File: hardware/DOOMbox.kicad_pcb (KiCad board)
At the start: 4 copper layers, 128 parts, among them J1 DE15_Socket_HighDensity, J2 AudioJack3, SW1 SW_SPST, SW2 SW_Push, U1 RPi Pico 2, U2 AP7381-50SA-7, U3 LM324N, U4 CD4010BE

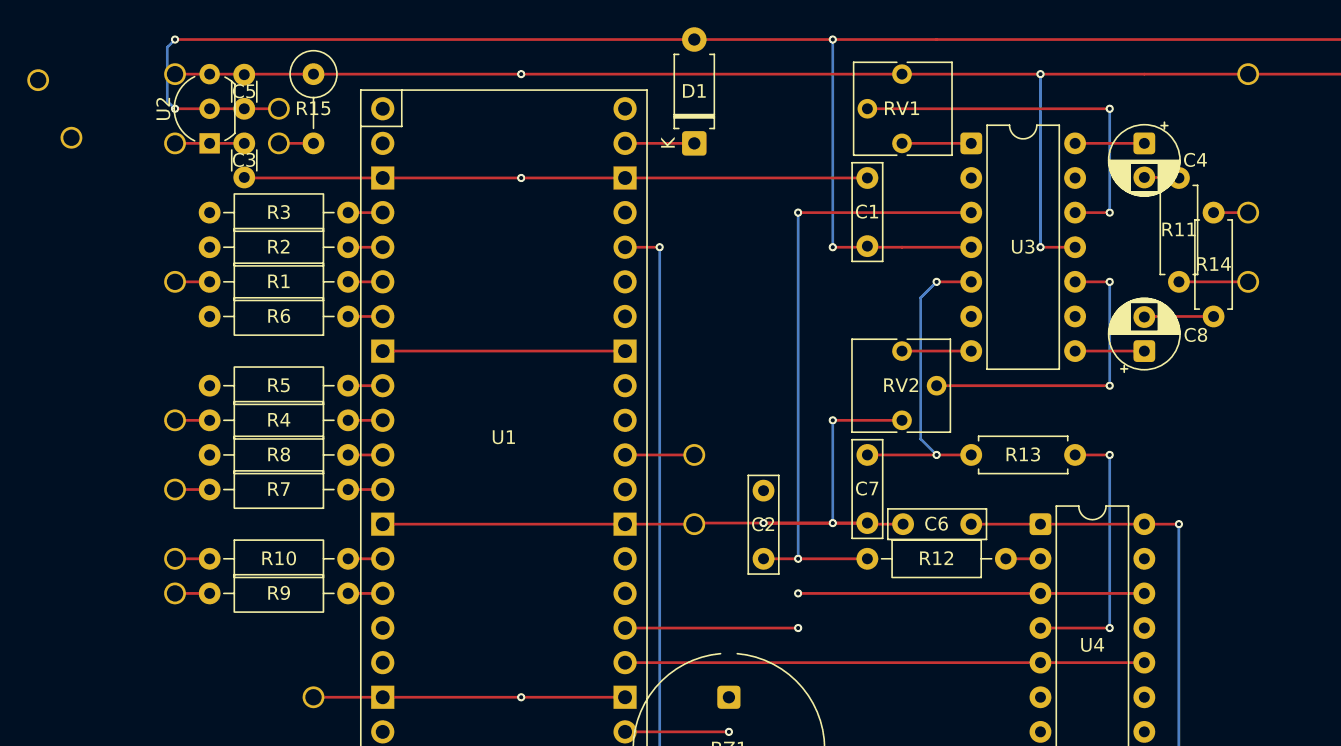
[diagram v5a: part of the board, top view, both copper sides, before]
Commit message: Fix incorrect pins on U2 and accidental stripboard cut in U4
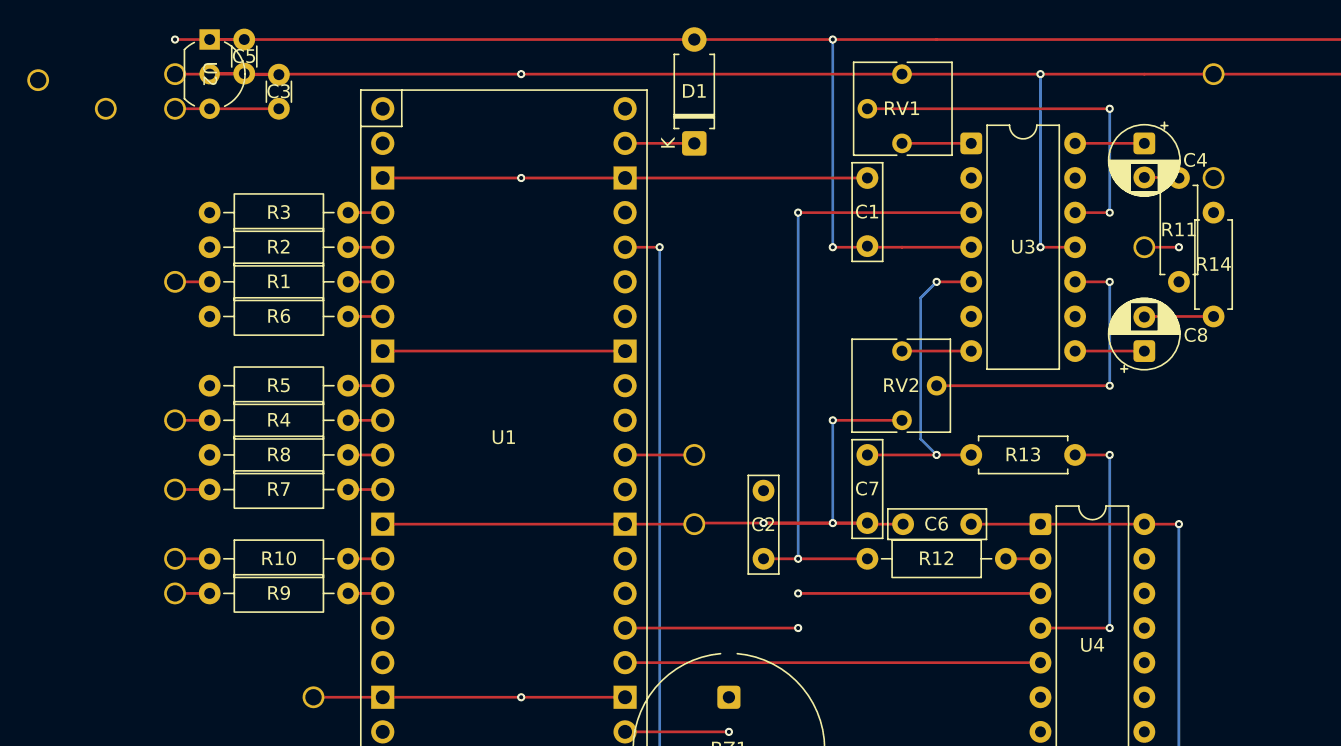
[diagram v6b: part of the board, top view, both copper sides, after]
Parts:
- removed D2 (x2): LED, Stripboard:Peripheral_Offboard
- removed R15: 15K, Resistor_THT:R_Axial_DIN0309_L9.0mm_D3.2mm_P5.08mm_Vertical
- removed the REF** at (116.8, 96.5)
- added REF**: Stripboard_Cut, Stripboard:Stripboard_Cut, F.Cu at (121.9, 66.0)
- added REF** (x2): Stripboard_Cut, Stripboard:Stripboard_Cut, F.Cu at (119.4, 68.6)
- added REF**: Stripboard_Cut, Stripboard:Stripboard_Cut, F.Cu at (125.7, 63.6)
- added REF**: Stripboard_Cut, Stripboard:Stripboard_Cut, F.Cu at (120.6, 96.5)
- U2: footprint Package_TO_SOT_THT:TO-92_Inline_Wide -> AP7381:AP7381-TO92
- moved J2 8.03 mm to (121.9, 68.6)
- moved C5 5.08 mm to (55.9, 53.3), turned to -90 degrees
- moved U2 5.08 mm to (53.3, 55.9), turned to -90 degrees
- moved C3 3.59 mm to (58.4, 58.4), turned to 90 degrees
- moved J2 3.59 mm to (127.0, 63.5)
- moved SW1 3.30 mm to (45.7, 58.4)
- moved SW1 2.54 mm to (50.8, 58.4)
- moved J2 2.54 mm to (127.0, 55.9)
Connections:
- U2 pad 1: Net-(SW1-B) -> +5V
- U2 pad 2: +5V -> GND
- U2 pad 3: GND -> Net-(SW1-B)
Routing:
- net +5V: track 130.0 -> 119.4 mm, vias 4 -> 3
- net PWM_AUR: track 38.1 -> 30.5 mm
- net PWM_AUL: track 40.6 -> 33.0 mm
- net GND: track 363.3 -> 358.2 mm
- net Net-(SW1-B): track 5.08 -> 7.62 mm
- net Net-(D2-K): track 2.54 -> 0.00 mm
- net Net-(J2-PadT): vias 0 -> 1
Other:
- board text removed: "D2"
